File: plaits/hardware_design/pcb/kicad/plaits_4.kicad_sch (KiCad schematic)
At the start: 58 parts

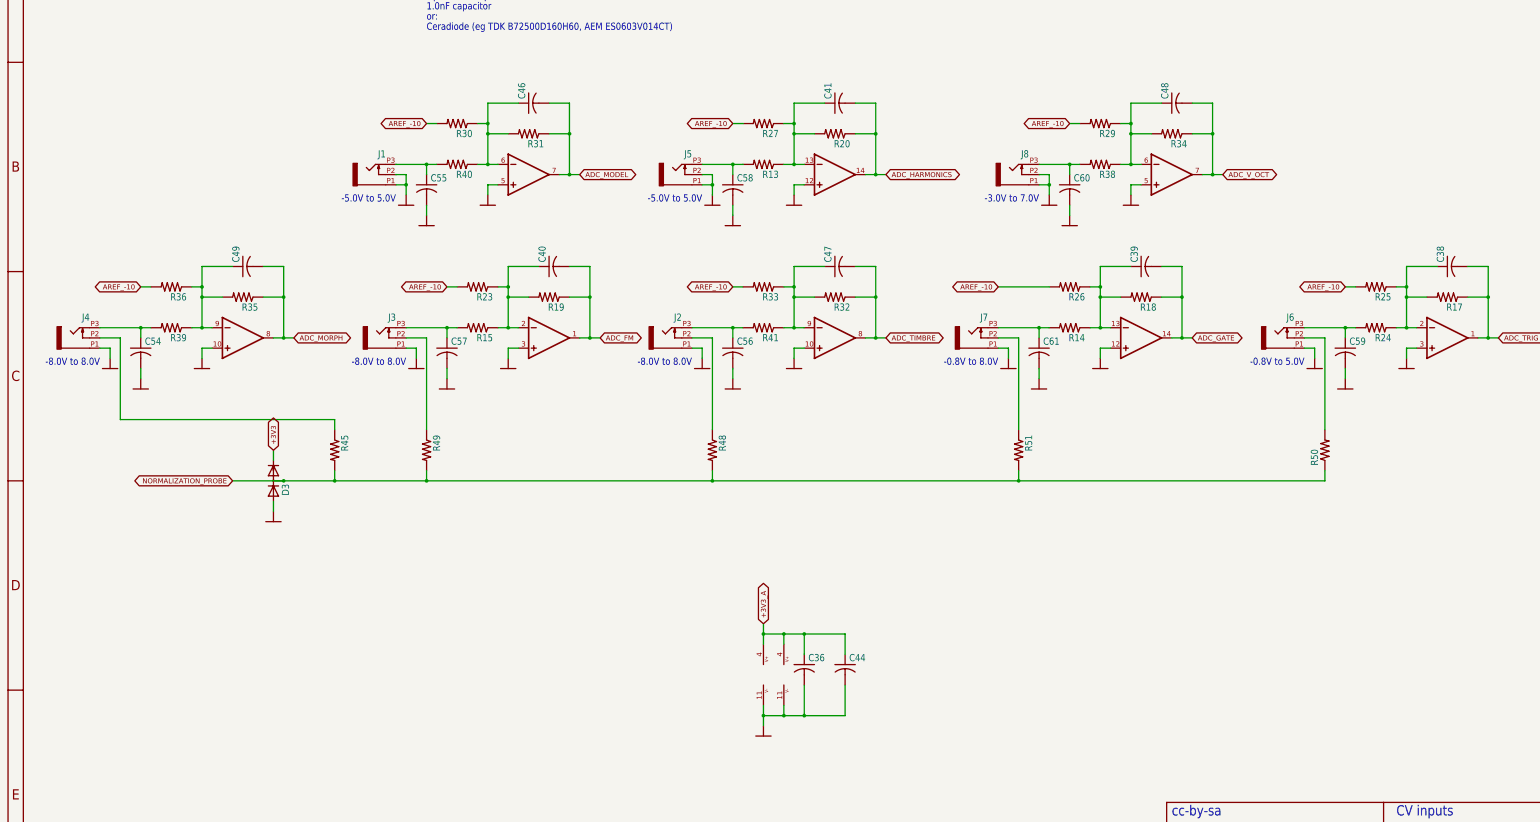
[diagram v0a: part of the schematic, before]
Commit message: plaits resized panasonic A -> B caps
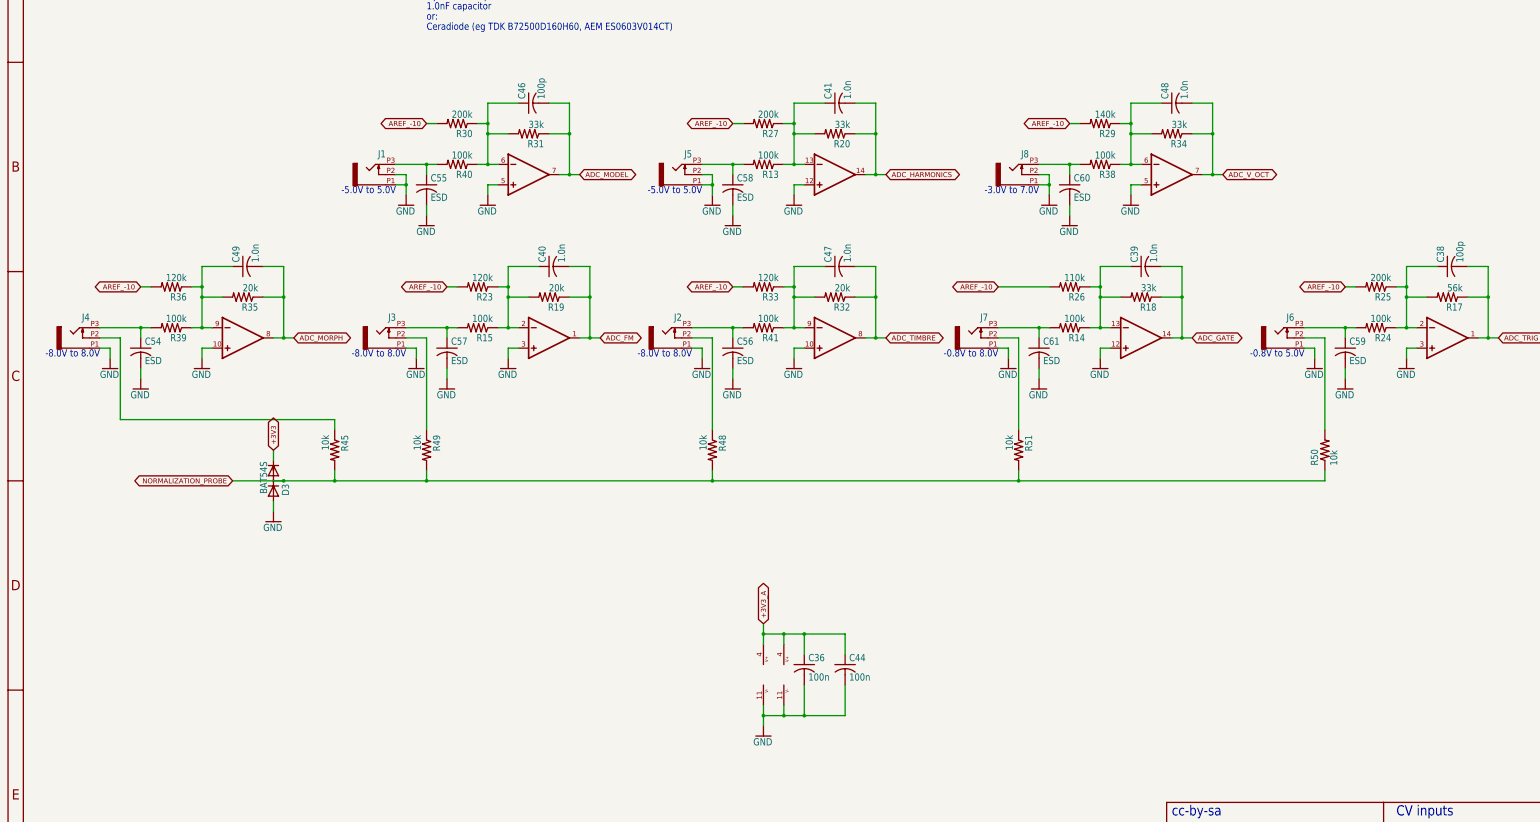
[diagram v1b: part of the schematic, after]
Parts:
- C36, C44: value (none) -> 100n; footprint (none) -> plaits:C0402
- C38, C46: value (none) -> 100p; footprint (none) -> plaits:C0402
- C39, C40, C41, C47, C48, C49: value (none) -> 1.0n; footprint (none) -> plaits:C0402
- C54, C55, C56, C57, C58, C59, C60, C61: value (none) -> ESD; footprint (none) -> plaits:C0603
- D3: value (none) -> BAT54S; footprint (none) -> plaits:SOT23
- IC6, IC7: value (none) -> MCP6004; footprint (none) -> plaits:TSSOP14_065
- J1, J2, J3, J4, J5, J6, J7, J8: value (none) -> PJ301_THONKICONN6; footprint (none) -> plaits:WQP_PJ_301M6
- R13, R14, R15, R24, R38, R39, R40, R41: value (none) -> 100k; footprint (none) -> plaits:R0402
- R17: value (none) -> 56k; footprint (none) -> plaits:R0402
- R18, R20, R31, R34: value (none) -> 33k; footprint (none) -> plaits:R0402
- R19, R32, R35: value (none) -> 20k; footprint (none) -> plaits:R0402
- R23, R33, R36: value (none) -> 120k; footprint (none) -> plaits:R0402
- R25, R27, R30: value (none) -> 200k; footprint (none) -> plaits:R0402
- R26: value (none) -> 110k; footprint (none) -> plaits:R0402
- R29: value (none) -> 140k; footprint (none) -> plaits:R0402
- R45, R48, R49, R50, R51: value (none) -> 10k; footprint (none) -> plaits:R0402
